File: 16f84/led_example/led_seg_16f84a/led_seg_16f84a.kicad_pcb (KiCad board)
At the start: 2 copper layers, 23 parts, among them J1 MTA06-156, Q1 20.0MHz, T1 BC337, T2 BC337, T3 BC337, T5 BC337, U1 CC56-12EWA, U3 PIC16F84A-XXP

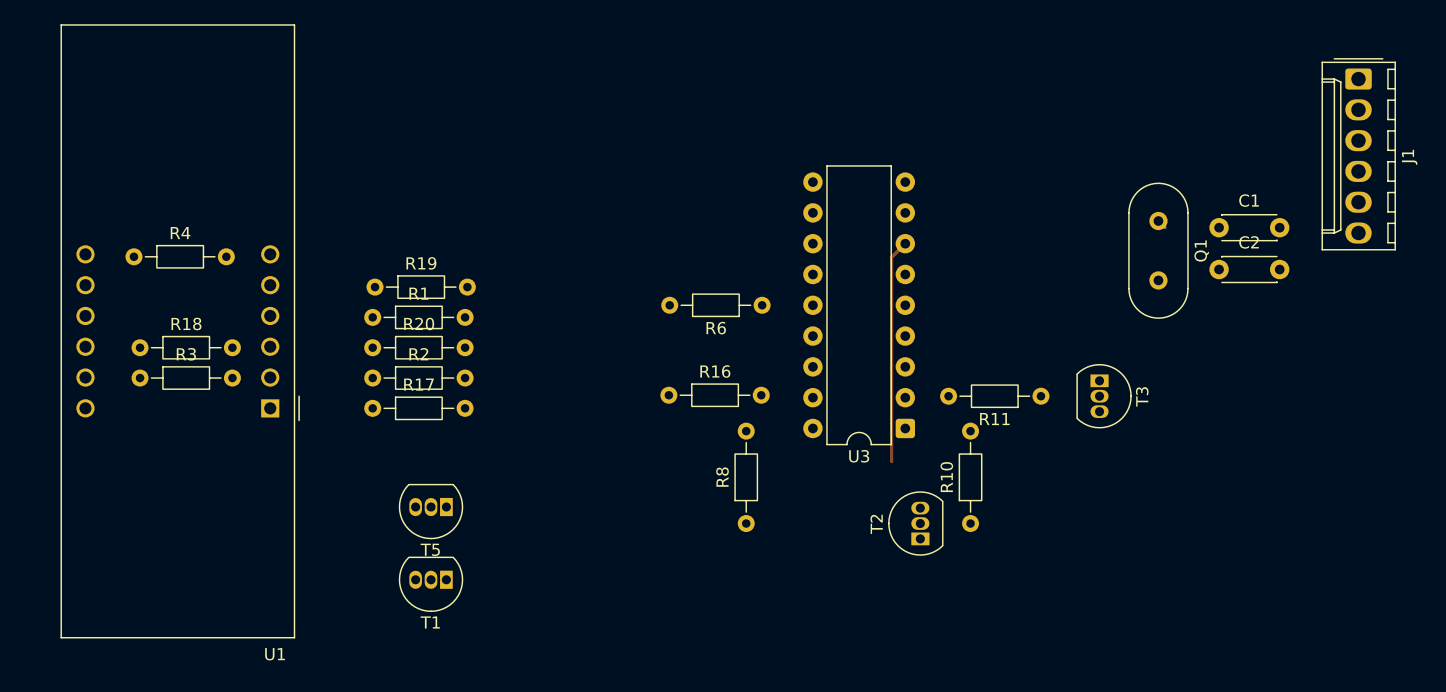
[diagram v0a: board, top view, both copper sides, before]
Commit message: 16f84a added ds18 project it uses only one sensor connected also updated ds18 absolute project for pic16f913
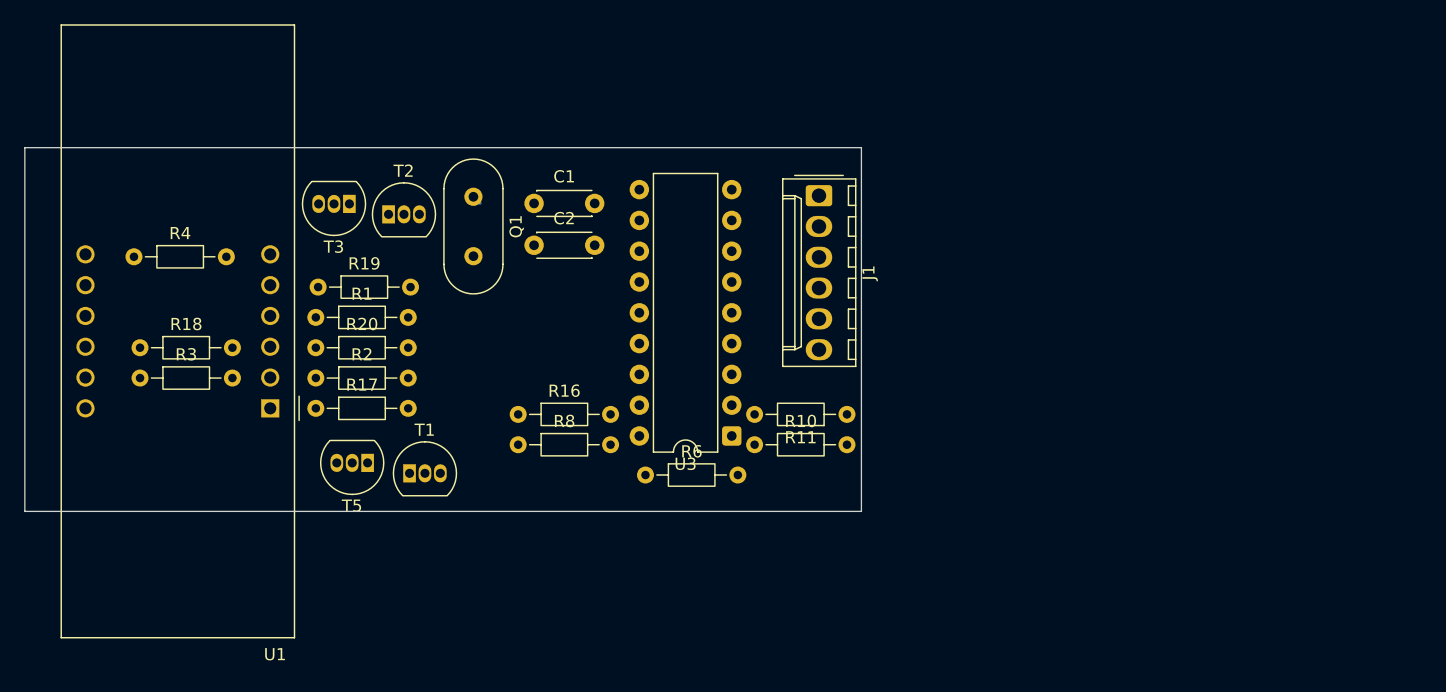
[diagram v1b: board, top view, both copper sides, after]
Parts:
- moved T3 63.6 mm to (131.8, 52.6), turned to 180 degrees
- moved C1 56.5 mm to (147.0, 52.6)
- moved C2 56.5 mm to (147.0, 56.0)
- moved Q1 56.5 mm to (142.0, 52.0)
- moved T2 51.4 mm to (135.0, 53.5), turned to 0 degrees
- moved J1 45.5 mm to (170.5, 52.0)
- moved R8 19.9 mm to (145.7, 72.5), turned to 0 degrees
- moved R10 19.0 mm to (165.2, 72.5), turned to 0 degrees
- moved R6 17.0 mm to (156.2, 75.0), turned to 0 degrees
- moved R11 16.1 mm to (172.8, 70.0)
- moved U3 14.3 mm to (163.3, 71.8)
- moved R16 12.5 mm to (145.7, 70.0)
- moved T1 9.29 mm to (136.7, 74.9), turned to 0 degrees
- moved T5 7.45 mm to (133.3, 74.0)
- moved R1 4.69 mm to (129.0, 62.0)
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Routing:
- net Net-(U3-RB1): track 18.4 -> 0.00 mm
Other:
- board outline added: 69 x 30 mm
